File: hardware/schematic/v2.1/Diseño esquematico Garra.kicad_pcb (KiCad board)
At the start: 2 copper layers, 85.5 x 137 mm, 21 parts

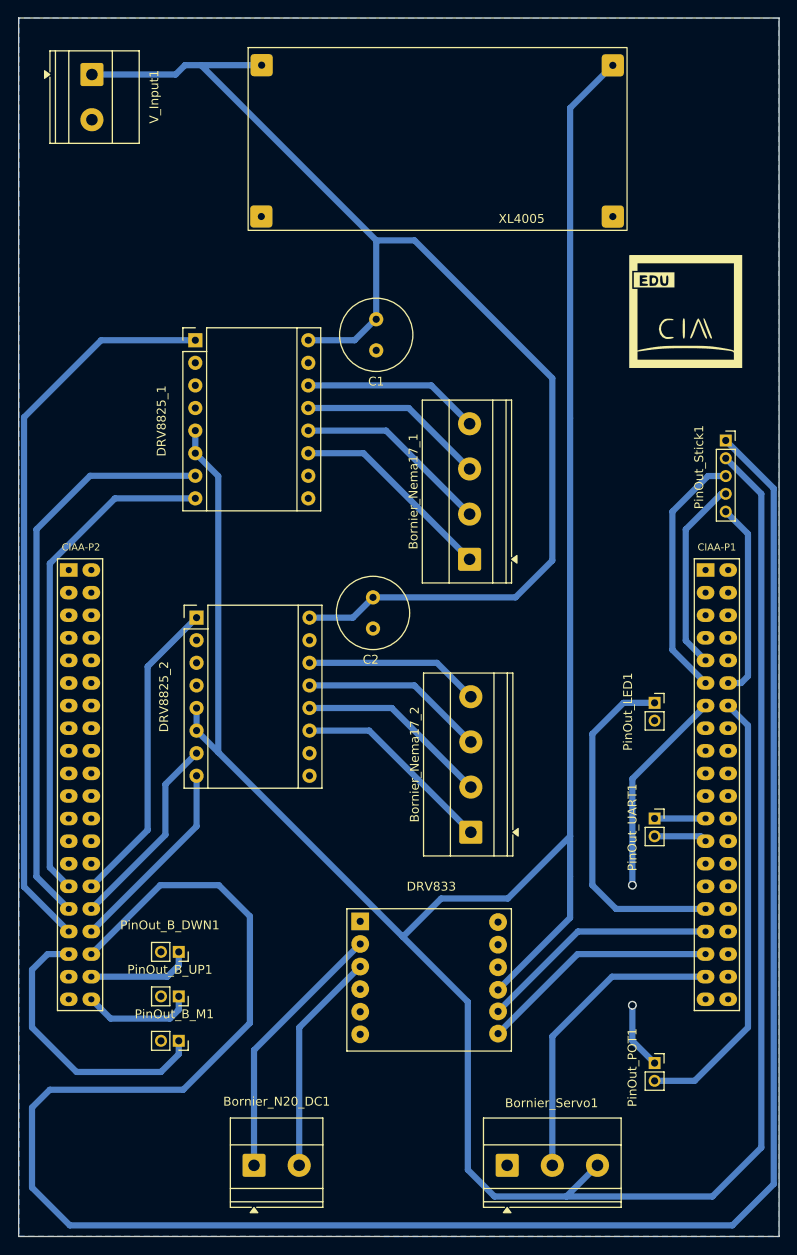
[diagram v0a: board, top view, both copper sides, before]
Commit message: feat: add through holes for connectivity & GNDs links
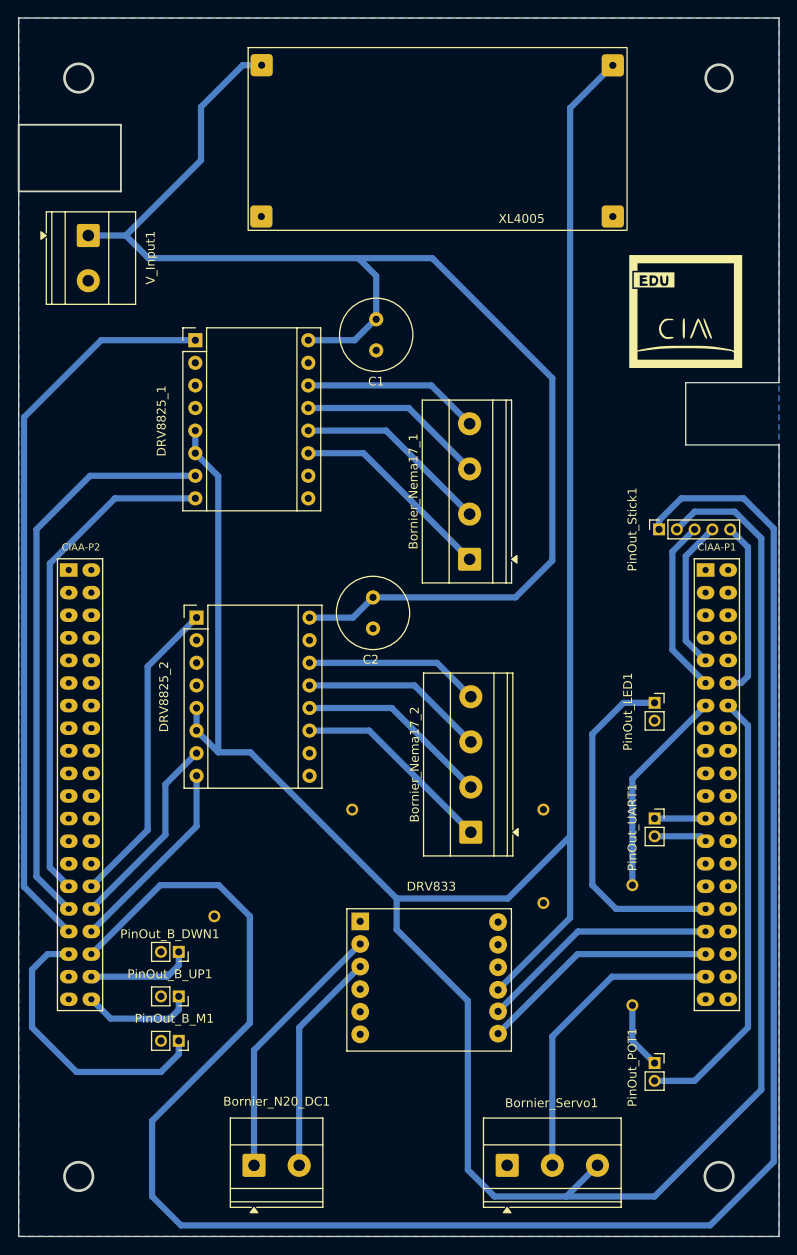
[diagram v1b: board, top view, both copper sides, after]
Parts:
- added ?: , , F.Cu at (72.5, 114.0)
- added ?: , , F.Cu at (57.0, 126.0)
- added ?: , , F.Cu at (94.0, 124.5)
- added ?: , , F.Cu at (104.0, 122.5)
- added ?: , , F.Cu at (104.0, 136.0)
- added ?: , , F.Cu at (94.0, 114.0)
- moved V_Input1 18.1 mm to (42.8, 49.5)
- moved PinOut_Stick1 12.5 mm to (107.0, 82.5), turned to 90 degrees
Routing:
- net SW: track 244.8 -> 220.3 mm
- net 12V: track 141.5 -> 152.3 mm
- net VRX: track 28.5 -> 19.9 mm
- net VRY: track 21.8 -> 16.9 mm
- net GND_Stick: track 22.1 -> 19.9 mm
- net 5V: track 355.2 -> 353.3 mm
- net POT: vias 2 -> 0
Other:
- outline, holes or cut-outs redrawn

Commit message: feat: hole diameter adjustment
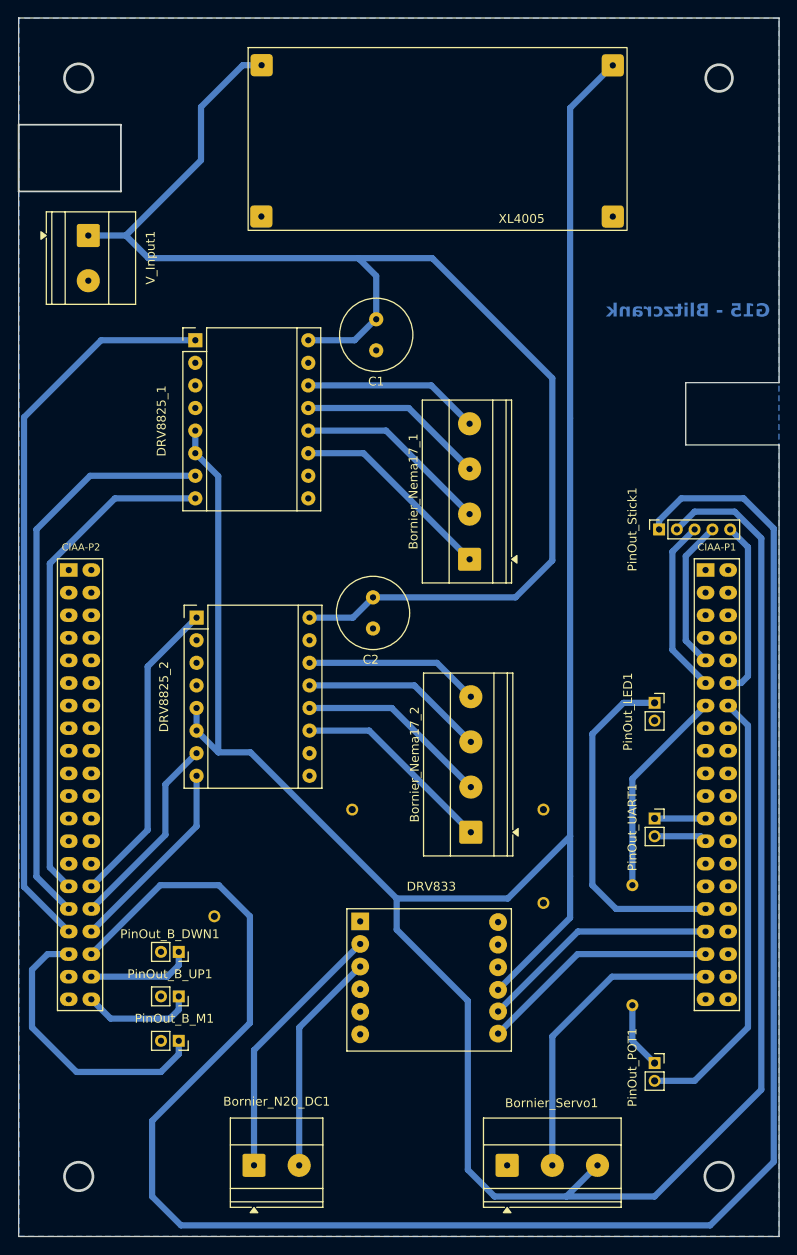
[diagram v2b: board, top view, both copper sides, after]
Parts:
- removed G***: LOGO, LIBRERIA_EDU_CIAA_NXP:LOGO
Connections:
- net SW renamed Stick_ON
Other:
- board text added: "G15 - Blitzcrank"

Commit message: fix: PDF
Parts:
- moved PinOut_B_M1 1.50 mm to (53.0, 141.5)
- moved PinOut_B_DWN1 1.25 mm to (53.0, 128.8)
- moved PinOut_B_UP1 0.50 mm to (53.0, 135.5)
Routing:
- net VRX: track 19.9 -> 23.5 mm
- net VRY: track 16.9 -> 19.9 mm
- net B_M: track 32.3 -> 31.0 mm
- net B_UP: track 12.9 -> 12.1 mm
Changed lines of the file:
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@@
 		(grid_origin 35 25)
 		(pcbplotparams
-			(layerselection 0x00000000_00000000_55555555_5755f5ff)
-			(plot_on_all_layers_selection 0x00000000_00000000_00000000_00000000)
+			(layerselection 0x00000000_00000000_55555555_55555554)
+			(plot_on_all_layers_selection 0x00000000_00000000_00000002_2200888c)
 			(disableapertmacros no)
 			(usegerberextensions no)
@@
 			(crossoutdnponfab yes)
 			(subtractmaskfromsilk no)
-			(outputformat 1)
+			(outputformat 4)
 			(mirror no)
-			(drillshape 1)
+			(drillshape 2)
 			(scaleselection 1)
-			(outputdirectory "")
+			(outputdirectory "/home/manuel/Documents/Facultad/blitzcrank/resources/PCB/v2.1/")
 		)
 	)
@@
 	(footprint "Connector_PinSocket_2.00mm:PinSocket_1x02_P2.00mm_Vertical"
 		(layer "F.Cu")
-		(at 53 135 -90)
+		(at 53 135.5 -90)
 		(descr "Through hole straight socket strip, 1x02, 2.00mm pitch, single row (from Kicad 4.0.7), script generated")
 		(tags "Through hole socket strip THT 1x02 2.00mm single row")
 		(property "Reference" "PinOut_B_UP1"
-			(at -2.5 1 0)
+			(at 2.5 0.75 0)
 			(layer "F.SilkS")
 			(effects
@@
 	(footprint "Connector_PinSocket_2.00mm:PinSocket_1x02_P2.00mm_Vertical"
 		(layer "F.Cu")
-		(at 53 140 -90)
+		(at 53 141.5 -90)
 		(descr "Through hole straight socket strip, 1x02, 2.00mm pitch, single row (from Kicad 4.0.7), script generated")
 		(tags "Through hole socket strip THT 1x02 2.00mm single row")
 		(property "Reference" "PinOut_B_M1"
-			(at -2.5 0.5 0)
+			(at 0 8.75 0)
 			(layer "F.SilkS")
 			(effects
@@
 	(footprint "Connector_PinSocket_2.00mm:PinSocket_1x02_P2.00mm_Vertical"
 		(layer "F.Cu")
-		(at 53 130 -90)
+		(at 53 128.75 -90)
 		(descr "Through hole straight socket strip, 1x02, 2.00mm pitch, single row (from Kicad 4.0.7), script generated")
 		(tags "Through hole socket strip THT 1x02 2.00mm single row")
 		(property "Reference" "PinOut_B_DWN1"
-			(at -2 1 0)
+			(at 2.5 0.75 0)
 			(layer "F.SilkS")
 			(effects
@@
 	)
 	(segment
+		(start 106 87.5)
+		(end 111 82.5)
+		(width 0.7)
+		(layer "B.Cu")
+		(net 17)
+	)
+	(segment
 		(start 112.23 99.77)
-		(end 108.5 96.04)
+		(end 109.52 99.77)
 		(width 0.7)
 		(layer "B.Cu")
@@
 	)
 	(segment
-		(start 108.5 96.04)
-		(end 108.5 85)
+		(start 106 96.25)
+		(end 106 87.5)
 		(width 0.7)
 		(layer "B.Cu")
@@
 	)
 	(segment
-		(start 108.5 85)
-		(end 111 82.5)
+		(start 109.52 99.77)
+		(end 106 96.25)
 		(width 0.7)
 		(layer "B.Cu")
@@
 	)
 	(segment
-		(start 110 85.5)
-		(end 113 82.5)
+		(start 109.98 97.23)
+		(end 108 95.25)
 		(width 0.7)
 		(layer "B.Cu")
@@
 	(segment
 		(start 112.23 97.23)
-		(end 110 95)
+		(end 109.98 97.23)
 		(width 0.7)
 		(layer "B.Cu")
@@
 	)
 	(segment
-		(start 110 95)
-		(end 110 85.5)
+		(start 108 95.25)
+		(end 108 87.5)
+		(width 0.7)
+		(layer "B.Cu")
+		(net 20)
+	)
+	(segment
+		(start 108 87.5)
+		(end 113 82.5)
 		(width 0.7)
 		(layer "B.Cu")
@@
 	)
 	(segment
-		(start 53 141.5)
-		(end 53 140)
+		(start 41.5 143.5)
+		(end 51.5 143.5)
 		(width 0.7)
 		(layer "B.Cu")
@@
 	)
 	(segment
-		(start 36.5 132)
-		(end 36.5 138.5)
+		(start 40.63 130.25)
+		(end 38.25 130.25)
 		(width 0.7)
 		(layer "B.Cu")
@@
 	)
 	(segment
-		(start 36.5 138.5)
-		(end 41.5 143.5)
+		(start 53 142)
+		(end 53 141.5)
 		(width 0.7)
 		(layer "B.Cu")
@@
 	)
 	(segment
-		(start 40.63 130.25)
-		(end 38.25 130.25)
+		(start 38.25 130.25)
+		(end 36.5 132)
 		(width 0.7)
 		(layer "B.Cu")
@@
 	)
 	(segment
-		(start 51 143.5)
-		(end 53 141.5)
+		(start 36.5 132)
+		(end 36.5 138.5)
 		(width 0.7)
 		(layer "B.Cu")
@@
 	)
 	(segment
-		(start 41.5 143.5)
-		(end 51 143.5)
+		(start 36.5 138.5)
+		(end 41.5 143.5)
 		(width 0.7)
 		(layer "B.Cu")
@@
 	)
 	(segment
-		(start 38.25 130.25)
-		(end 36.5 132)
+		(start 51.5 143.5)
+		(end 53 142)
 		(width 0.7)
 		(layer "B.Cu")
@@
 	)
 	(segment
-		(start 51.71 132.79)
-		(end 53 131.5)
+		(start 43.21 132.75)
+		(end 50.25 132.75)
 		(width 0.7)
 		(layer "B.Cu")
@@
 	)
 	(segment
-		(start 53 131.5)
+		(start 50.25 132.75)
 		(end 53 130)
 		(width 0.7)
@@
 	(segment
 		(start 43.17 132.79)
-		(end 51.71 132.79)
+		(end 43.21 132.75)
 		(width 0.7)
 		(layer "B.Cu")
@@
 	)
 	(segment
-		(start 43.17 135.33)
-		(end 45.34 137.5)
+		(start 53 130)
+		(end 53 128.75)
+		(width 0.7)
+		(layer "B.Cu")
+		(net 81)
+	)
+	(segment
+		(start 43.17 135.42)
+		(end 45 137.25)
 		(width 0.7)
 		(layer "B.Cu")
@@
 	)
 	(segment
-		(start 52 137.5)
-		(end 53 136.5)
+		(start 43.17 135.33)
+		(end 43.17 135.42)
 		(width 0.7)
 		(layer "B.Cu")
@@
 	)
 	(segment
-		(start 45.34 137.5)
-		(end 52 137.5)
+		(start 45 137.25)
+		(end 52 137.25)
 		(width 0.7)
 		(layer "B.Cu")
@@
 	)
 	(segment
-		(start 53 136.5)
-		(end 53 135)
+		(start 52 137.25)
+		(end 53 136.25)
 		(width 0.7)
 		(layer "B.Cu")
@@
 		(layer "B.Cu")
 		(net 82)
+	)
+	(segment
+		(start 53 136.25)
+		(end 53 135.5)
+		(width 0.7)
+		(layer "B.Cu")
+		(net 82)
